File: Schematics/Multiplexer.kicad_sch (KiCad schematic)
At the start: 53 parts, among them J10 Conn_01x02, J11 Conn_01x02, J12 Conn_01x02, J13 Conn_01x02, J14 Conn_01x02, J15 Conn_01x02, J16 Conn_01x02, J17 Conn_01x02, J5 Conn_01x02, J6 Conn_01x03, J7 Conn_01x02, J8 Conn_01x02, J9 Conn_01x02, U10 DG212C, U11 DG212C, U12 DG212C, U13 DG212C, U14 DG212C, U15 DG212C, U5 DG212C, U6 DG212C, U7 DG212C, U8 DG212C, U9 DG212C

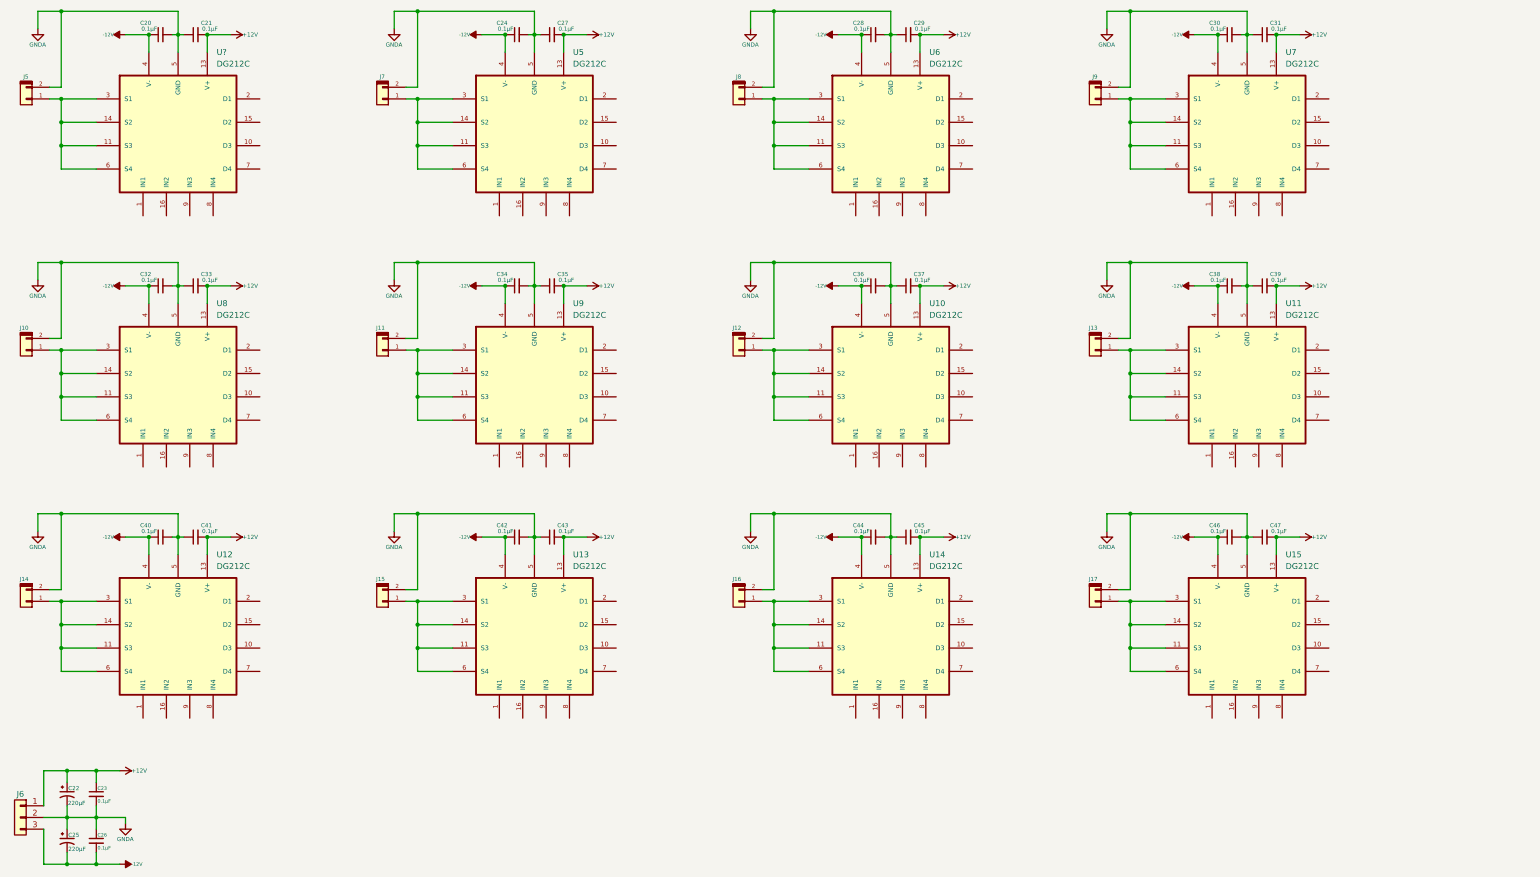
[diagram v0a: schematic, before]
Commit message: partial rework of 3 state filter and display to 7 inches.
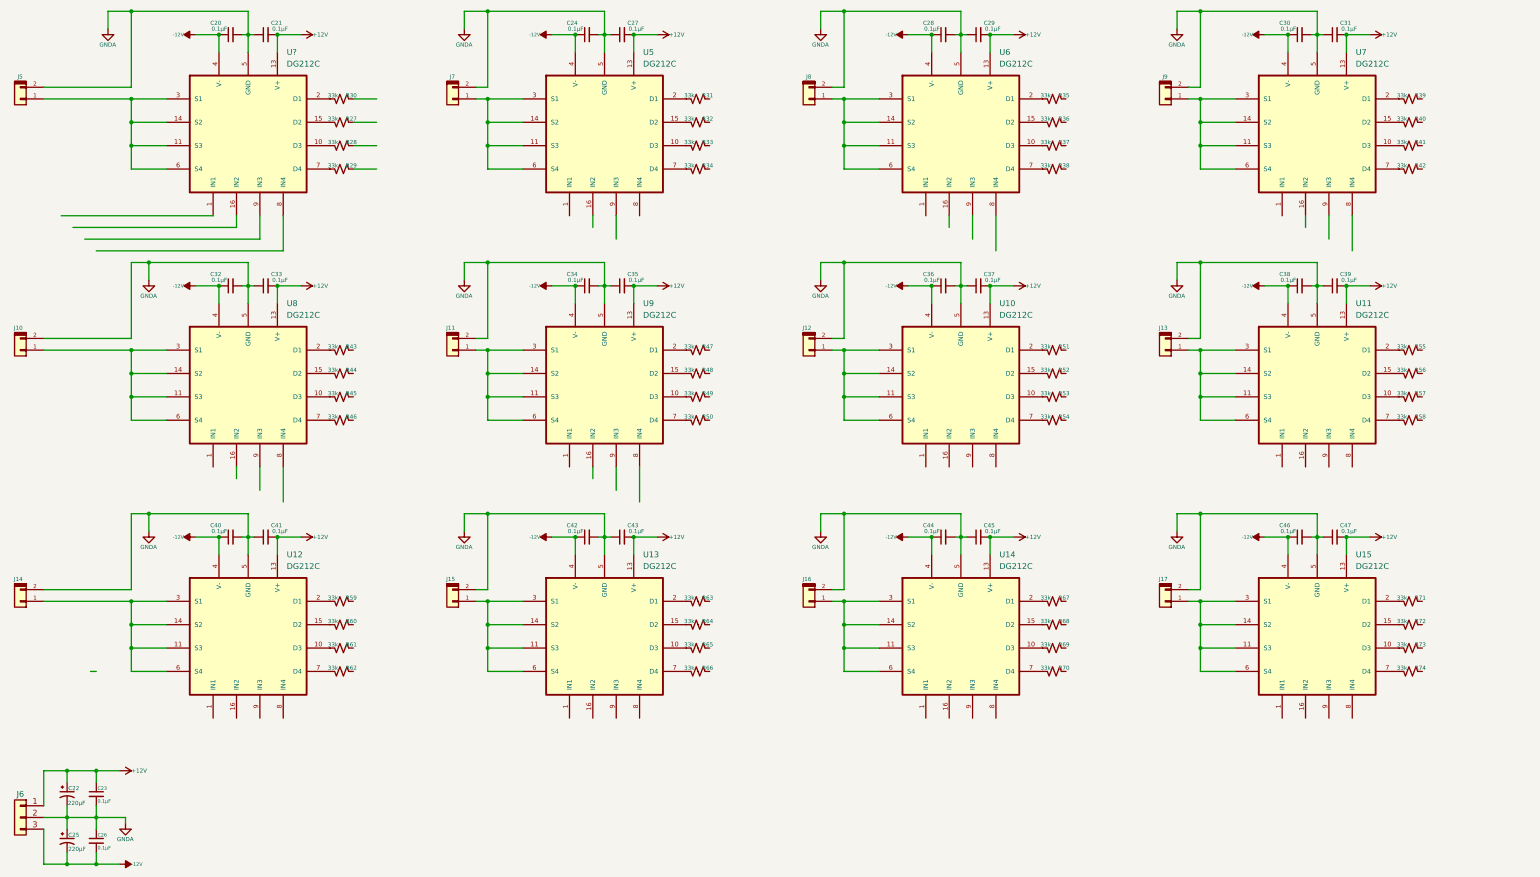
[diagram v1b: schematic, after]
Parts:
- added R27, R28, R29, R30, R31, R32, R33, R34, R35, R36, R37, R38, R39, R40, R41, R42, R43, R44, R45, R46, R47, R48, R49, R50, R51, R52, R53, R54, R55, R56, R57, R58, R59, R60, R61, R62, R63, R64, R65, R66, R67, R68, R69, R70, R71, R72, R73, R74: 33k, symbol Device:R_Small_US
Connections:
- net at U?.10 (D3): now also R28.2
- net at U?.15 (D2): now also R27.2
- net at U?.2 (D1): now also R30.2
- net at U?.7 (D4): now also R29.2
- net at U15.10 (D3): now also R73.2
- net at U15.15 (D2): now also R72.2
- net at U15.2 (D1): now also R71.2
- net at U15.7 (D4): now also R74.2
- net at U13.10 (D3): now also R65.2
- net at U13.15 (D2): now also R64.2
- net at U13.2 (D1): now also R63.2
- net at U13.7 (D4): now also R66.2
- net at U9.10 (D3): now also R49.2
- net at U9.15 (D2): now also R48.2
- net at U9.2 (D1): now also R47.2
- net at U9.7 (D4): now also R50.2
- net at U8.10 (D3): now also R45.2
- net at U8.15 (D2): now also R44.2
- net at U8.2 (D1): now also R43.2
- net at U8.7 (D4): now also R46.2
- net at U10.10 (D3): now also R53.2
- net at U10.15 (D2): now also R52.2
- net at U10.2 (D1): now also R51.2
- net at U10.7 (D4): now also R54.2
- net at U14.10 (D3): now also R69.2
- net at U14.15 (D2): now also R68.2
- net at U14.2 (D1): now also R67.2
- net at U14.7 (D4): now also R70.2
- net at U5.10 (D3): now also R33.2
- net at U5.15 (D2): now also R32.2
- net at U5.2 (D1): now also R31.2
- net at U5.7 (D4): now also R34.2
- net at U11.10 (D3): now also R57.2
- net at U11.15 (D2): now also R56.2
- net at U11.2 (D1): now also R55.2
- net at U11.7 (D4): now also R58.2
- net at U6.10 (D3): now also R37.2
- net at U6.15 (D2): now also R36.2
- net at U6.2 (D1): now also R35.2
- net at U6.7 (D4): now also R38.2
- net at U12.10 (D3): now also R61.2
- net at U12.15 (D2): now also R60.2
- net at U12.2 (D1): now also R59.2
- net at U12.7 (D4): now also R62.2
- net at U7.10 (D3): now also R41.2
- net at U7.15 (D2): now also R40.2
- net at U7.2 (D1): now also R39.2
- net at U7.7 (D4): now also R42.2
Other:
- moved on the sheet: C20, C21, C24, C27, C28, C29, C30, C31, C32, C33, C34, C35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

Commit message: updated schematics.
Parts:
- removed C34, C35, C36, C37, C38, C39, C40, C41, C42, C43, C44, C45, C46, C47: 0.1µF, symbol Device:C_Small
- removed J10, J11, J12, J13, J14, J15, J16, J17, J5, J7, J9: Conn_01x02, symbol My Connectors:Conn_01x02
- removed R37, R40, R41, R42, R61, R62, R63, R64, R65, R66, R67, R68, R69, R70, R71, R72, R73, R74: 33k, symbol Device:R_Small_US
- removed U10, U12, U13, U14, U15, U8, U9, U?: DG212C, symbol My Chips:DG212C
- added C34: 100pF, symbol Resistors:C_Small
- added J5, J7, J76, J77, J78, J79, J80, J90: Conn_01x04, symbol My Connectors:Conn_01x04
- added J9: Conn_01x03, symbol My Connectors:Conn_01x03
- added JP2, JP3, JP4: Jumper_2_Small_Open, symbol Jumper:Jumper_2_Small_Open
- added Q11, Q12: BSS138, digikey-footprints:SOT-23-3, symbol dk_Transistors-FETs-MOSFETs-Single:BSS138
- added U10: TL072, symbol Amplifier_Operational:TL072
- added U8: PCF8575, Package_SO:SSOP-24_5.3x8.2mm_P0.65mm, symbol Interface_Expansion:PCF8575DBR
- added U9: LM1117-3.3, symbol Regulator_Linear:LM1117-3.3
- C32, C33: value 0.1µF -> .1µF
- R27, R28, R29, R43, R44, R45, R46, R47, R48, R49, R50, R51, R52, R53, R54, R55, R56, R57, R58: value 33k -> 10K
- R59, R60: value 33k -> 10k
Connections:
- net +12V: now also U10.8 (V+); no longer C33.2
- net -12V: now also U10.4 (V-); no longer C32.1
- net GNDA: now also C33.2, J5.1 (Pin_1), J5.3 (Pin_3), J7.2 (Pin_2), J7.4 (Pin_4), J76.1 (Pin_1), J76.3 (Pin_3), J77.2 (Pin_2), J77.4 (Pin_4), J78.1 (Pin_1), J78.3 (Pin_3), J79.2 (Pin_2), J79.4 (Pin_4), J80.1 (Pin_1), J80.3 (Pin_3), J9.1 (Pin_1), J90.2 (Pin_2), J90.4 (Pin_4), JP2.1 (A), JP3.1 (A), JP4.1 (A), U10.3 (+), U8.12 (GND), U9.1 (GND); no longer C33.1
- net at U7.7 (D4): now also R32.1
- net at R28.2: now also JP3.2 (B), U8.2 (A1)
- net at R27.2: now also JP4.2 (B), U8.3 (A2)
- net at R30.2: now also J8.1 (Pin_1), C34.1, U10.1
- net at R29.2: now also JP2.2 (B), U8.21 (A0)
- net at U7.15 (D2): now also R33.1
- net at R58.1: now also U7.8 (IN4), U8.20 (P17)
- net at R58.2: now also C33.1, R27.1, R28.1, R29.1, R43.1, R44.1, R45.1, R46.1, R47.1, R48.1, R49.1, R50.1, R51.2, R52.2, R53.2, R54.2, R55.2, R56.2, R57.2, R59.2, R60.2, Q11.1, Q12.1, U8.24 (VCC), U9.2 (VO); no longer U11.7 (D4)
- net at R51.1: now also U11.1 (IN1), U8.13 (P10)
- net at R49.2: now also U6.9 (IN3), U8.10 (P6)
- net at R56.1: now also U7.16 (IN2), U8.18 (P15)
- net Direct 5: now reaches U11.15 (D2)
- net Direct 5: no longer R56.2
- net at R46.2: now also U5.8 (IN4), U8.7 (P3)
- net at R53.1: now also U11.9 (IN3), U8.15 (P12)
- net Direct 2: now reaches R35.1
- net Direct 2: now also U5.7 (D4)
- net at R35.2: now also R30.1, R31.2, R32.2, R33.2, R34.2, R36.2, R38.2, R39.2, C34.2, U10.2 (-); no longer U6.2 (D1)
- net at R60.1: now also Q12.2, U8.23 (SDA)
- net at R43.2: now also U5.1 (IN1), U8.4 (P0)
- net Direct 1: now reaches R34.1
- net Direct 1: now also U5.15 (D2)
- net Audio 1A: now reaches U5.14 (S2), U5.3 (S1)
- net Audio 1A: now also J76.4 (Pin_4), J77.1 (Pin_1); no longer U5.11 (S3), U5.6 (S4)
- net Direct 3: now reaches R36.1
- net at U6.15 (D2): now also R38.1; no longer R36.2
- net at R52.1: now also U11.16 (IN2), U8.14 (P11)
- net at R48.2: now also U6.16 (IN2), U8.9 (P5)
- net at R47.2: now also U6.1 (IN1), U8.8 (P4)
- net at R50.2: now also U6.8 (IN4), U8.11 (P7)
- net at R45.2: now also U5.9 (IN3), U8.6 (P2)
- net at R44.2: now also U5.16 (IN2), U8.5 (P1)
- net Filter 4: now reaches U6.10 (D3)
- net Filter 2: now reaches U5.10 (D3)
- net Filter 2: no longer R33.2
- net Filter 1: now reaches U5.2 (D1)
- net Filter 1: no longer R31.2
- net Filter 8: now reaches U7.10 (D3)
- net Filter 6: now reaches U11.10 (D3)
- net Filter 6: no longer R57.2
- net Audio 2A: now reaches U11.14 (S2), U11.3 (S1)
- net Audio 2A: now also J80.4 (Pin_4), J90.1 (Pin_1); no longer U11.11 (S3), U11.6 (S4)
- net Filter 5: now reaches U11.2 (D1)
- net Filter 5: no longer R55.2
- net at U11.8 (IN4): now also R54.1, U8.16 (P13)
- net at R39.1: now also U6.7 (D4)
- net Filter 7: now reaches U7.2 (D1)
- net Filter 7: no longer R39.2
- net at R57.1: now also U7.9 (IN3), U8.19 (P16)
- net Direct 4: now reaches R31.1
- net at R55.1: now also U7.1 (IN1), U8.17 (P14)
- net at R59.1: now also Q11.2, U8.22 (SCL)
- net Audio 2C: now reaches U7.14 (S2), U7.3 (S1)
- net Audio 2C: now also J78.4 (Pin_4), J79.1 (Pin_1); no longer U7.11 (S3), U7.6 (S4)
- new net +12: C32.1, U9.3 (VI)
- new net +3.3: U11.12 (VL), U5.12 (VL), U6.12 (VL), U7.12 (VL)
- new net Audio 1B: J76.2 (Pin_2), J77.3 (Pin_3), U5.11 (S3), U5.6 (S4)
- new net Audio 1C: J5.4 (Pin_4), J7.1 (Pin_1), U6.14 (S2), U6.3 (S1)
- new net Audio 1D: J5.2 (Pin_2), J7.3 (Pin_3), U6.11 (S3), U6.6 (S4)
- new net Audio 2B: J80.2 (Pin_2), J90.3 (Pin_3), U11.11 (S3), U11.6 (S4)
- new net Audio 2D: J78.2 (Pin_2), J79.3 (Pin_3), U7.11 (S3), U7.6 (S4)
- new net Direct 6: U11.7 (D4)
- new net Filter 3: U6.2 (D1)
- new net SCL0: J9.3 (Pin_3), Q11.3
- new net SDA0: J9.2 (Pin_2), Q12.3
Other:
- note added: "A0"
- note added: "A1"
- note added: "A2"
- note added: "Direct out To mixer"
- moved on the sheet: C20, C21, C22, C23, C24, C25, C26, C27, C28, C29, C30, C31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

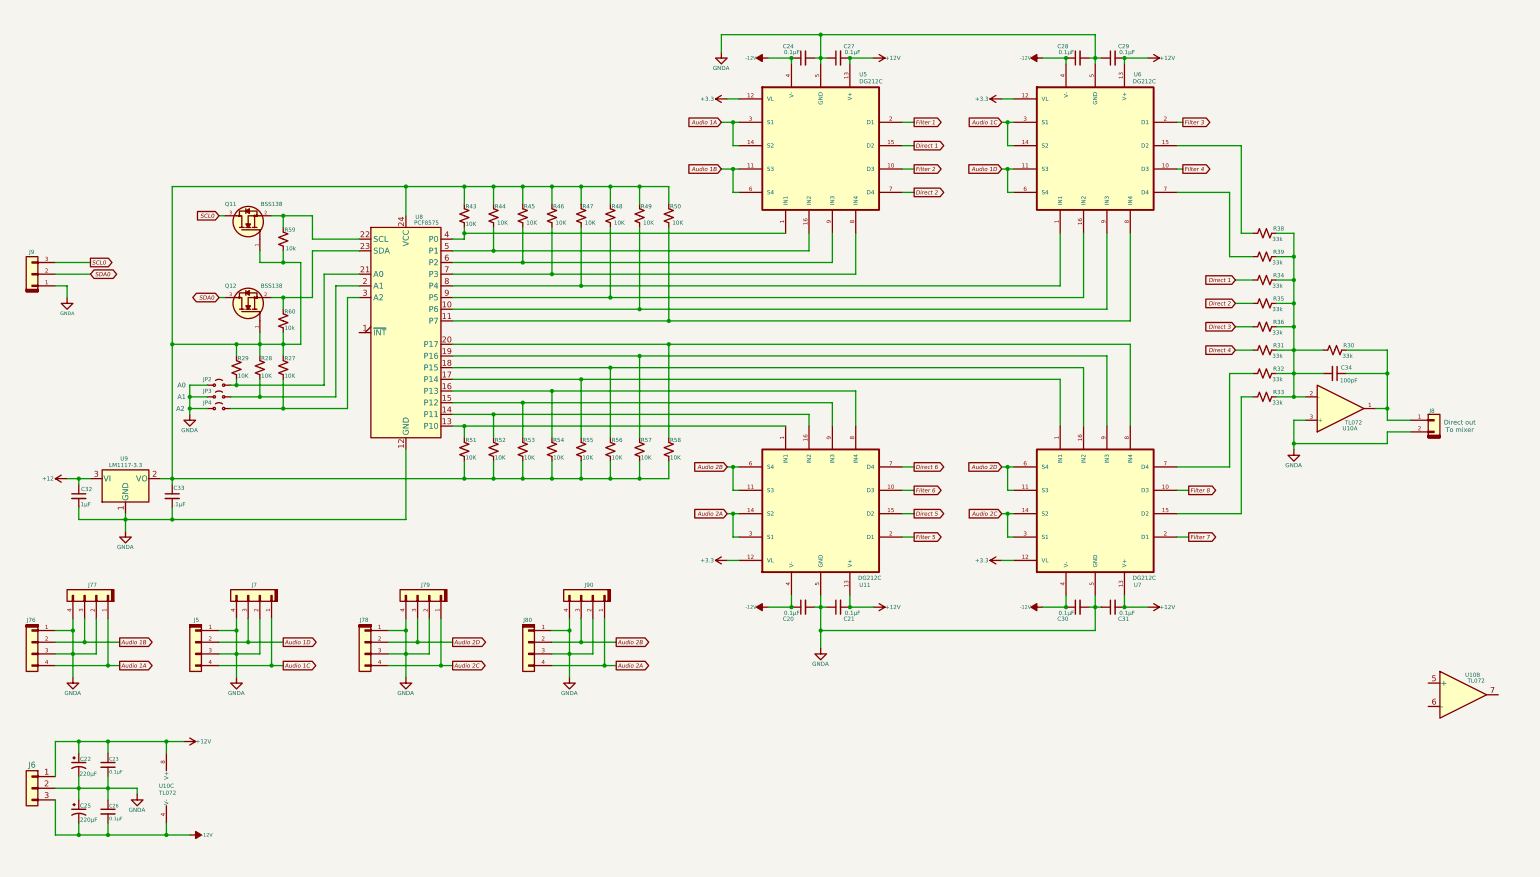
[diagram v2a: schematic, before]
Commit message: Added first level audio mux and fixed tuning control.
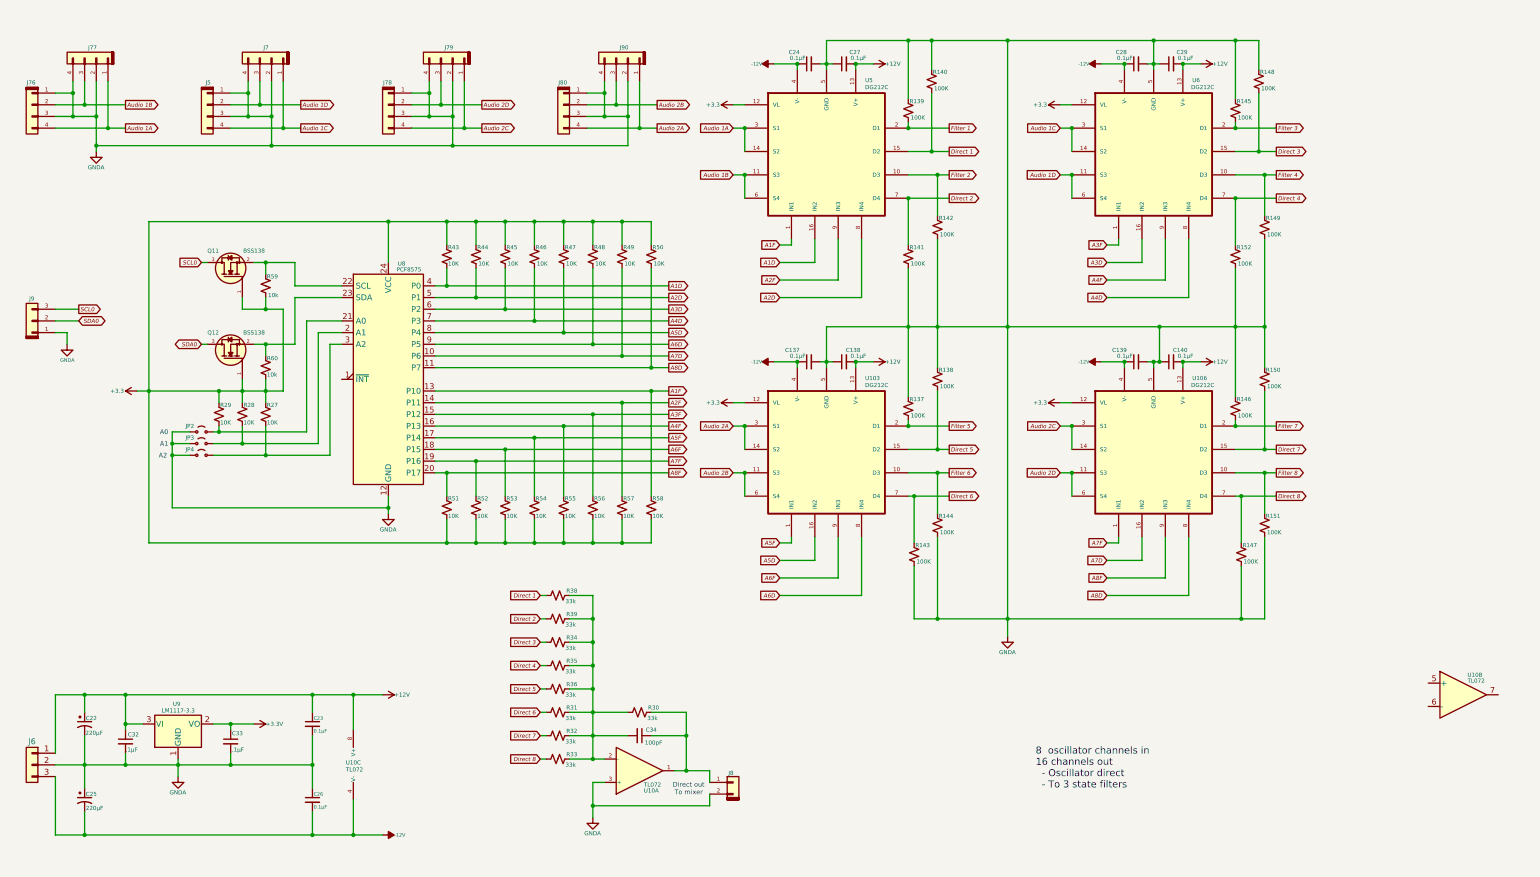
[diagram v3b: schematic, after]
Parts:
- removed C20, C21, C30, C31: 0.1µF, symbol Device:C_Small
- removed U11, U7: DG212C, symbol My Chips:DG212C
- added C137, C138, C139, C140: 0.1µF, symbol Device:C_Small
- added R137, R138, R139, R140, R141, R142, R143, R144, R145, R146, R147, R148, R149, R150, R151, R152: 100K, symbol Device:R_Small_US
- added U103, U106: DG212C, symbol My Chips:DG212C
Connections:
- net +12 is gone; now on net +12V: C32.1, U9.3 (VI)
- net +12V: now also C138.2, C140.2, U103.13 (V+), U106.13 (V+)
- net +3.3: now also Q11.1, Q12.1, R27.1, R28.1, R29.1, R43.1, R44.1, R45.1, R46.1, R47.1, R48.1, R49.1, R50.1, R51.2, R52.2, R53.2, R54.2, R55.2, R56.2, R57.2, R58.2, R59.2, R60.2, U8.24 (VCC), U103.12 (VL), U106.12 (VL)
- net -12V: now also C137.1, C139.1, U103.4 (V-), U106.4 (V-)
- net Audio 2A: now also U103.14 (S2), U103.3 (S1)
- net Audio 2B: now also U103.11 (S3), U103.6 (S4)
- net Audio 2C: now also U106.14 (S2), U106.3 (S1)
- net Audio 2D: now also U106.11 (S3), U106.6 (S4)
- net Direct 1: now also R38.1, R140.2; no longer R34.1
- net Direct 2: now also R39.1, R141.1; no longer R35.1
- net Direct 3: now also R34.1, U6.15 (D2), R148.2; no longer R36.1
- net Direct 4: now also R35.1, U6.7 (D4), R152.1; no longer R31.1
- net Direct 5: now also R36.1, R138.2, U103.15 (D2)
- net Direct 6: now also R31.1, R143.1, U103.7 (D4)
- net Filter 1: now also R139.2
- net Filter 2: now also R142.1
- net Filter 3: now also R145.2
- net Filter 4: now also R149.1
- net Filter 5: now also R137.2, U103.2 (D1)
- net Filter 6: now also R144.1, U103.10 (D3)
- net Filter 7: now also R146.2, U106.2 (D1)
- net Filter 8: now also R151.1, U106.10 (D3)
- net GNDA: now also C137.2, C138.1, C139.2, C140.1, R137.1, R138.1, R139.1, R140.1, R141.2, R142.2, R143.2, R144.2, R145.1, R146.1, R147.2, R148.1, R149.2, R150.1, R151.2, R152.2, U103.5 (GND), U106.5 (GND)
- net A2F: now reaches U8.14 (P11)
- net A2F: now also R57.1, U5.9 (IN3); no longer R52.1
- net A1F: now reaches R58.1
- net A1F: now also U5.1 (IN1), U8.13 (P10); no longer U8.20 (P17)
- net A8F: now reaches R51.1
- net A8F: now also U8.20 (P17), U106.9 (IN3); no longer U8.13 (P10)
- net A4F: now reaches U8.16 (P13)
- net A4F: now also R55.1, U6.9 (IN3); no longer R54.1
- net A3F: now reaches U8.15 (P12)
- net A3F: now also R56.1, U6.1 (IN1); no longer R53.1
- net A7D: now reaches R49.2, U8.10 (P6)
- net A7D: now also U106.16 (IN2); no longer U6.9 (IN3)
- net A1D: now reaches R43.2, U8.4 (P0)
- net A1D: now also U5.16 (IN2); no longer U5.1 (IN1)
- net A5D: now reaches R47.2, U8.8 (P4)
- net A5D: now also U103.16 (IN2); no longer U6.1 (IN1)
- net A4D: now reaches R46.2, U8.7 (P3)
- net A4D: now also U6.8 (IN4); no longer U5.8 (IN4)
- net A3D: now reaches R45.2, U8.6 (P2)
- net A3D: now also U6.16 (IN2); no longer U5.9 (IN3)
- net A8D: now reaches R50.2, U8.11 (P7)
- net A8D: now also U106.8 (IN4); no longer U6.8 (IN4)
- net A5F: now reaches U8.17 (P14)
- net A5F: now also R54.1, U103.1 (IN1); no longer R55.1
- net A6F: now reaches U8.18 (P15)
- net A6F: now also R53.1, U103.9 (IN3); no longer R56.1
- net A7F: now reaches U8.19 (P16)
- net A7F: now also R52.1, U106.1 (IN1); no longer R57.1
- net A2D: now reaches R44.2, U8.5 (P1)
- net A2D: now also U5.8 (IN4); no longer U5.16 (IN2)
- net A6D: now reaches R48.2, U8.9 (P5)
- net A6D: now also U103.8 (IN4); no longer U6.16 (IN2)
- net Direct 7: now reaches R32.1
- net Direct 7: now also R150.2, U106.15 (D2)
- net Direct 8: now reaches R33.1
- net Direct 8: now also R147.1, U106.7 (D4)
- new net +3.3V: C33.1, U9.2 (VO)
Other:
- note added: "8 oscillator channels in 16 channels out - Oscillator direct - To 3 state filters"
- moved on the sheet: C22, C23, C24, C25, C26, C27, C28, C29, C32, C33, C34, J5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

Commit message: Prelude to split configurations.
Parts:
- added C142, C143: .1µF, symbol Device:C_Small
- added U72: LM1117-3.3, symbol Regulator_Linear:LM1117-3.3
- U9: value LM1117-3.3 -> LM1117-5
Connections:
- net +3.3 is gone; now on net +3.3V: Q11.1, Q12.1, R27.1, R28.1, R29.1, R43.1, R44.1, R45.1, R46.1, R47.1, R48.1, R49.1, R50.1, R51.2, R52.2, R53.2, R54.2, R55.2, R56.2, R57.2, R58.2, R59.2, R60.2, U103.12 (VL), U106.12 (VL), U5.12 (VL), U6.12 (VL), U8.24 (VCC)
- net +3.3V: now also C143.1, U72.2 (VO); no longer C33.1, U9.2 (VO)
- net GNDA: now also C142.2, C143.2, U72.1 (GND)
- new net +5V: C142.1, C33.1, U72.3 (VI), U9.2 (VO)
